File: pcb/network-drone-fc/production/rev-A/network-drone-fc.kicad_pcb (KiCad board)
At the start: 4 copper layers, 36 x 39 mm, 85 parts, among them J1 U.FL-R-SMT-1, J2 TYPE-C 16PIN 2MD, J3 U.FL GPS, J4 ESC, J5 Sensor port 5V I2C, J6 Radio UART 5V, J7 Charging board, J8 Landing sensor 5V I2C, U1 ESP32-S3FN8, U2 USBLC6-2SC6, U3 AP63205WU-7, U4 TLV75733PDRVR, U5 TPS7A2033PDBVR, U6 ICM-42688-P, U7 BMP581, U8 MAX-M10S, X1 Q22FA12800101

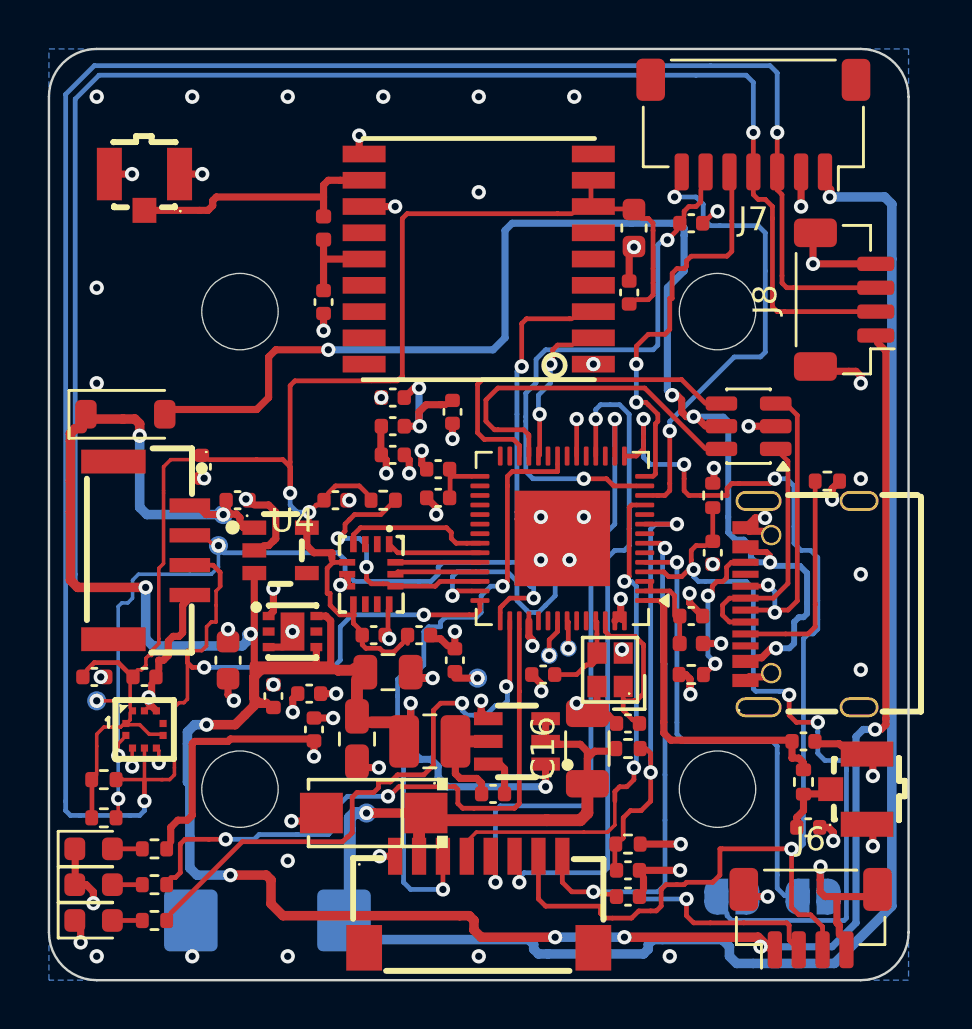
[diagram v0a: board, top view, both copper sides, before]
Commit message: Rev A order files regenerated: new parts, bottom-side assembly notes, assembly pictures
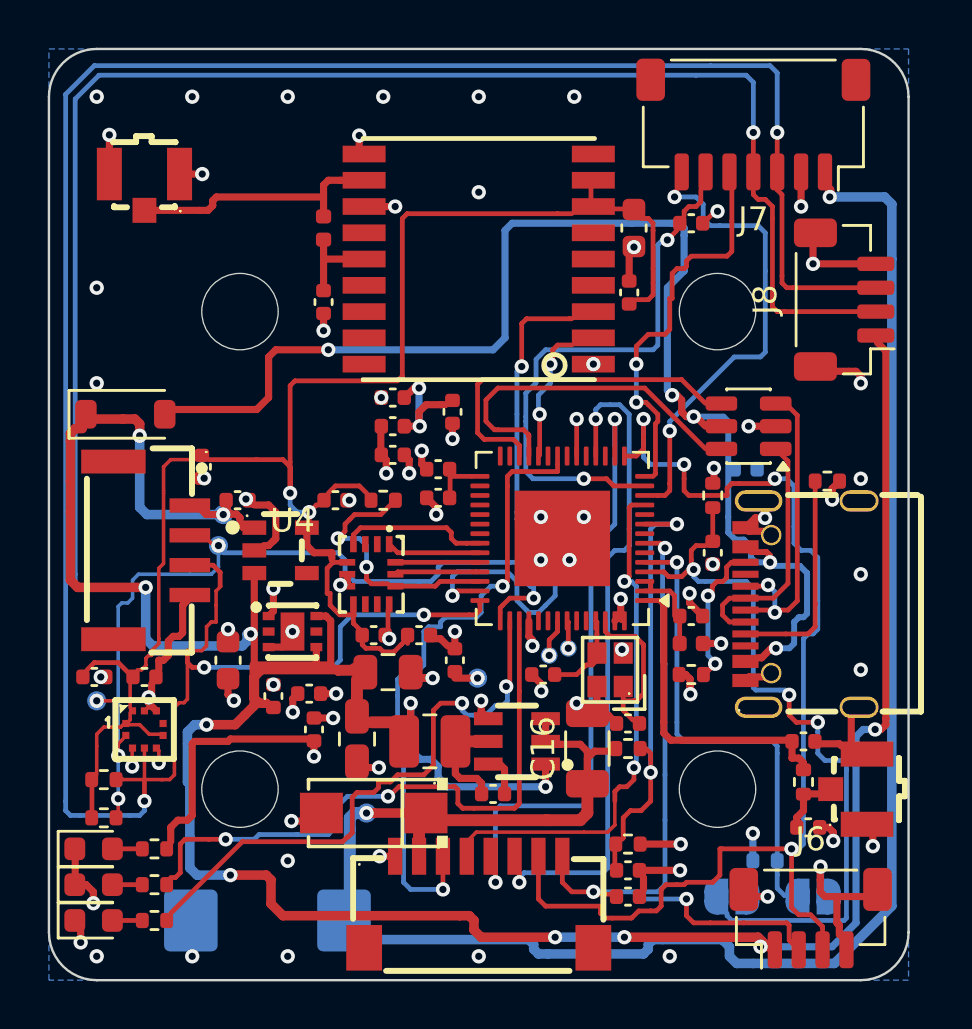
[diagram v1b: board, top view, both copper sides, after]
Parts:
- added C36: 100nF, Capacitor_SMD:C_0402_1005Metric, B.Cu at (111.2, 96.6)
- added R16: 10k, Resistor_SMD:R_0402_1005Metric, B.Cu at (112.0, 113.0)
- C18, C19: value 22uF 10V -> 22uF 16V
- D1: value B5819W -> 1N5819HW
- D5: value SMAJ18A -> SMAJ12A
- X1: value Q22FA12800101 -> FA-128 40MHz 10pF
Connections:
- net Net-(JP2-B) renamed BOOT
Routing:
- net +3V3: track 21.0 -> 22.2 mm, vias 13 -> 14
- net GND: vias 76 -> 75

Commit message: Rev A order files regenerated: gerbers, stencil, board copy, schematic PDF, assembly pictures
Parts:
- added C37: 1uF, Capacitor_SMD:C_0402_1005Metric, B.Cu at (106.0, 103.1)
- added C38: 0.1uF, Capacitor_SMD:C_0402_1005Metric, B.Cu at (101.3, 104.0)
- added C39: 0.1uF, Capacitor_SMD:C_0402_1005Metric, B.Cu at (103.5, 95.2)
- added L4: 24nH, Inductor_SMD:L_0402_1005Metric, F.Cu at (107.0, 105.0)
- added R14: 143k, Resistor_SMD:R_0402_1005Metric, B.Cu at (103.7, 108.5)
- added R15: 34k, Resistor_SMD:R_0402_1005Metric, B.Cu at (101.8, 106.9)
- C16: footprint Capacitor_SMD:C_1206_3216Metric -> Capacitor_SMD:C_0805_2012Metric
- moved C16 0.20 mm to (104.8, 108.3)
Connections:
- U1 pad 54: XTAL_P -> XTAL_P_CHIP
- U3 pad 2: VBAT -> BUCK_EN
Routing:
- net XTAL_P: track 6.92 -> 3.11 mm
- net BUCK_EN: track 0.00 -> 3.39 mm, vias 0 -> 1
- net XTAL_P_CHIP: track 0.00 -> 2.85 mm
- net GND: track 67.8 -> 70.4 mm
- net +3V3: track 22.2 -> 23.8 mm
- net Green: track 25.4 -> 26.0 mm
- net VBAT: track 79.3 -> 79.1 mm, vias 2 -> 3

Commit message: Rev A order files regenerated after the pre-order review: gerbers, stencil, board copy, schematic PDF, assembly pictures
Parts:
- added C40: 10uF, Capacitor_SMD:C_0603_1608Metric, B.Cu at (109.5, 97.6)
- moved D5 0.10 mm to (95.6, 110.9)
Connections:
- U6 pad 10: unconnected-(U6-RESV-Pad10) -> GND
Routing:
- net GND: track 70.4 -> 74.9 mm, vias 75 -> 74

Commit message: Rev A order files regenerated after the second round: gerbers, stencil, board copy, assembly pictures
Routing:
- net GND: track 74.9 -> 78.9 mm, vias 74 -> 103
- net +3V3: track 24.3 -> 25.4 mm

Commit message: Rev A gerbers, board copy and bottom assembly map regenerated with the test pad labels
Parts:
- added TP14: GND, TestPoint:TestPoint_Pad_D1.0mm, B.Cu at (94.0, 106.0)
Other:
- board text added: "3V3"
- board text added: "3V3S"
- board text added: "5V"
- board text added: "GND"
- board text added: "RX"
- board text added: "SCL"
- board text added: "TX"
- board text added: "VBAT"
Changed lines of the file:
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@@
 		(embedded_fonts no)
 	)
+	(footprint "TestPoint:TestPoint_Pad_D1.0mm"
+		(layer "B.Cu")
+		(at 94.03 106 180)
+		(descr "SMD pad as test Point, diameter 1.0mm")
+		(tags "test point SMD pad")
+		(property "Reference" "TP14"
+			(at 0 1.448 0)
+			(layer "B.SilkS")
+			(hide yes)
+			(effects
+				(font
+					(size 1 1)
+					(thickness 0.15)
+				)
+				(justify mirror)
+			)
+		)
+		(property "Value" "GND"
+			(at 0 -1.55 0)
+			(layer "B.Fab")
+			(hide yes)
+			(effects
+				(font
+					(size 1 1)
+					(thickness 0.15)
+				)
+				(justify mirror)
+			)
+		)
+		(property "Datasheet" ""
+			(at 0 0 0)
+			(unlocked yes)
+			(layer "B.Fab")
+			(hide yes)
+			(effects
+				(font
+					(size 1.27 1.27)
+					(thickness 0.15)
+				)
+				(justify mirror)
+			)
+		)
+		(property "Description" ""
+			(at 0 0 0)
+			(unlocked yes)
+			(layer "B.Fab")
+			(hide yes)
+			(effects
+				(font
+					(size 1.27 1.27)
+					(thickness 0.15)
+				)
+				(justify mirror)
+			)
+		)
+		(attr board_only exclude_from_pos_files exclude_from_bom)
+		(fp_circle
+			(center 0 0)
+			(end 0 -0.7)
+			(stroke
+				(width 0.12)
+				(type solid)
+			)
+			(fill no)
+			(layer "B.SilkS")
+		)
+		(fp_circle
+			(center 0 0)
+			(end 1 0)
+			(stroke
+				(width 0.05)
+				(type solid)
+			)
+			(fill no)
+			(layer "B.CrtYd")
+		)
+		(fp_text user "${REFERENCE}"
+			(at 0 1.45 0)
+			(layer "B.Fab")
+			(effects
+				(font
+					(size 1 1)
+					(thickness 0.15)
+				)
+				(justify mirror)
+			)
+		)
+		(pad "1" smd circle
+			(at 0 0 180)
+			(size 1 1)
+			(layers "B.Cu" "B.Mask")
+			(net 2 "GND")
+		)
+		(embedded_fonts no)
+	)
 	(gr_arc
 		(start 116 79)
@@
 		(layer "Edge.Cuts")
 	)
+	(gr_text "3V3S"
+		(at 84.388228 107.748888 0)
+		(layer "B.SilkS")
+		(effects
+			(font
+				(size 0.8 0.8)
+				(thickness 0.15)
+			)
+			(justify mirror)
+		)
+	)
+	(gr_text "RX"
+		(at 103.75 102.649999 0)
+		(layer "B.SilkS")
+		(effects
+			(font
+				(size 0.8 0.8)
+				(thickness 0.15)
+			)
+			(justify mirror)
+		)
+	)
+	(gr_text "GND"
+		(at 94.03 107.45 0)
+		(layer "B.SilkS")
+		(effects
+			(font
+				(size 0.8 0.8)
+				(thickness 0.15)
+			)
+			(justify mirror)
+		)
+	)
+	(gr_text "TX"
+		(at 103.338228 105.848888 0)
+		(layer "B.SilkS")
+		(effects
+			(font
+				(size 0.8 0.8)
+				(thickness 0.15)
+			)
+			(justify mirror)
+		)
+	)
+	(gr_text "5V"
+		(at 89.3 97.05 0)
+		(layer "B.SilkS")
+		(effects
+			(font
+				(size 0.8 0.8)
+				(thickness 0.15)
+			)
+			(justify mirror)
+		)
+	)
+	(gr_text "3V3"
+		(at 99.95 106.8 0)
+		(layer "B.SilkS")
+		(effects
+			(font
+				(size 0.8 0.8)
+				(thickness 0.15)
+			)
+			(justify mirror)
+		)
+	)
 	(gr_text "TAR Team 1  network drone FC  rev A"
 		(at 100 93.5 0)
@@
 		)
 	)
+	(gr_text "SCL"
+		(at 89.1 101.25 0)
+		(layer "B.SilkS")
+		(effects
+			(font
+				(size 0.8 0.8)
+				(thickness 0.15)
+			)
+			(justify mirror)
+		)
+	)
 	(gr_text "Pranav Shivashankar"
 		(at 100 92.2 0)
@@
 		)
 	)
+	(gr_text "VBAT"
+		(at 95.3 112.45 0)
+		(layer "B.SilkS")
+		(effects
+			(font
+				(size 0.8 0.8)
+				(thickness 0.15)
+			)
+			(justify mirror)
+		)
+	)
 	(segment
 		(start 114.09 102.263963)
@@
 	)
 	(segment
+		(start 86.276 104.4)
+		(end 86.18 104.4)
+		(width 0.15)
+		(layer "F.Cu")
+		(net 12)
+	)
+	(segment
 		(start 86.8 97.6)
 		(end 86.8 100.55)
@@
 	)
 	(segment
-		(start 86.3 104.2)
-		(end 86.3 104.4)
-		(width 0.15)
-		(layer "F.Cu")
-		(net 12)
-	)
-	(segment
 		(start 93.3 98.1)
 		(end 93.2 98.1)
@@
 	)
 	(segment
+		(start 86.5 104)
+		(end 86.5 104.176)
+		(width 0.15)
+		(layer "F.Cu")
+		(net 12)
+	)
+	(segment
 		(start 87.1 96.2)
 		(end 86.8 96.5)
@@
 	(segment
 		(start 86.6 103.9)
-		(end 86.3 104.2)
+		(end 86.5 104)
 		(width 0.15)
 		(layer "F.Cu")
@@
 	)
 	(segment
+		(start 86.5 104.176)
+		(end 86.276 104.4)
+		(width 0.15)
+		(layer "F.Cu")
+		(net 12)
+	)
+	(segment
 		(start 106.6 89.5)
 		(end 107.1 89.5)
@@
 		(layer "F.Cu")
 		(net 12)
-	)
-	(segment
-		(start 86.3 104.4)
-		(end 86.18 104.4)
-		(width 0.15)
-		(layer "F.Cu")
-		(net 12)
